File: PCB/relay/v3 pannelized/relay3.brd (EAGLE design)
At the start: 55.9 x 67.3 mm, 16 parts, among them K1 JS-M1-9V-5, K2 JS-M1-9V-5, Q1 BSP75, X1 22-23-20315.08S, X2 22-23-20315.08S

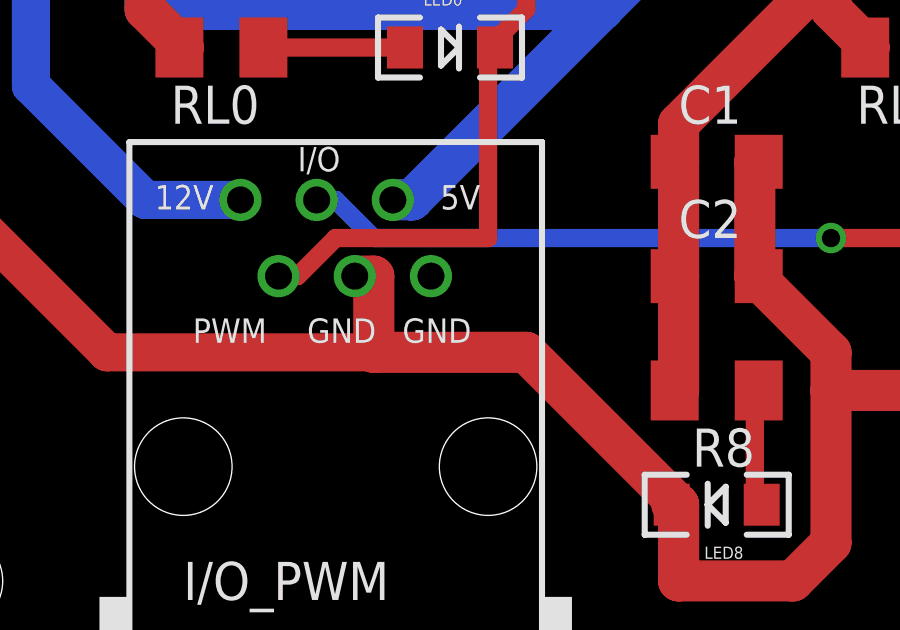
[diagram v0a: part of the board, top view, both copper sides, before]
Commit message: created GERBER files for integratedBertha, anemometer, relay3, door locking pcb. Changed CAM processor file (corrected a bug in silk layer, added a job with univalle/EPFL logos on bottom side).
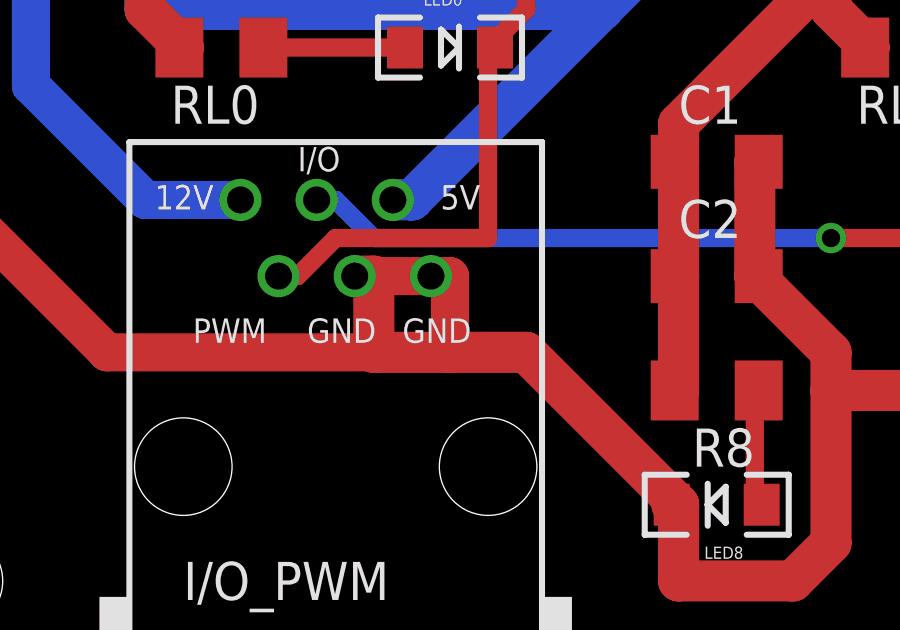
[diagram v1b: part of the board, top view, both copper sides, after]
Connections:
- net GND: now also I/O_PWM.GND1
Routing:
- net GND: track 83.7 -> 88.8 mm
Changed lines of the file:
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@@
 <wire x1="30.48" y1="13.97" x2="30.61" y2="13.97" width="1.3716" layer="1"/>
 <wire x1="22.86" y1="11.43" x2="27.94" y2="6.35" width="1.3716" layer="1"/>
-<wire x1="17.78" y1="11.43" x2="22.86" y2="11.43" width="1.3716" layer="1"/>
+<wire x1="17.78" y1="11.43" x2="20.32" y2="11.43" width="1.3716" layer="1"/>
+<wire x1="20.32" y1="11.43" x2="22.86" y2="11.43" width="1.3716" layer="1"/>
 <wire x1="17.78" y1="13.97" x2="17.78" y2="11.43" width="1.3716" layer="1"/>
 <wire x1="17.78" y1="13.97" x2="17.145" y2="13.97" width="1.3716" layer="1"/>
@@
 <wire x1="8.89" y1="11.43" x2="3.81" y2="16.51" width="1.27" layer="1"/>
 <wire x1="3.81" y1="16.51" x2="3.81" y2="39.37" width="1.27" layer="1"/>
+<contactref element="I/O_PWM" pad="GND1"/>
+<wire x1="19.685" y1="13.97" x2="20.32" y2="13.97" width="1.27" layer="1"/>
+<wire x1="20.32" y1="13.97" x2="20.32" y2="11.43" width="1.27" layer="1"/>
+<wire x1="17.78" y1="13.97" x2="19.685" y2="13.97" width="1.27" layer="1"/>
 </signal>
 <signal name="+5V" class="2">
